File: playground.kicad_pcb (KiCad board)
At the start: 2 copper layers, 50 x 50 mm, 20 parts, among them IC1 TXU0101DBVR, IC3 TXU0101DBVR, IC4 TXU0101DBVR, IC5 TXU0101DBVR, IC6 TXU0101DBVR, IC7 TXU0101DBVR, IC8 TXU0101DBVR, J1 USB_A, SW1 SW_DIP_x01, U2 ATSAMD21G18A-A

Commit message: updates
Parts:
- removed J1: USB_A, Connector_USB:USB3_A_Receptacle_Wuerth_692122030100
- added C3: 10u, Capacitor_SMD:C_0805_2012Metric, F.Cu at (153.4, 64.9)
- added C4: 10u, Capacitor_SMD:C_0805_2012Metric, F.Cu at (153.4, 67.9)
- added C5: 100n, Capacitor_SMD:C_0805_2012Metric, F.Cu at (153.4, 71.0)
- added C6: 100n, Capacitor_SMD:C_0805_2012Metric, F.Cu at (153.4, 74.0)
- added C7: 33p, Capacitor_SMD:C_0805_2012Metric, F.Cu at (153.4, 77.0)
- added C8: 22u, Capacitor_SMD:C_0805_2012Metric, F.Cu at (153.4, 80.0)
- added C9: 100n, Capacitor_SMD:C_0805_2012Metric, F.Cu at (153.4, 83.0)
- added IC10: TPS562242DRLR, Package_SO:MSOP-10_3x3mm_P0.5mm, F.Cu at (156.8, 96.0)
- added IC2: TXU0101DBVR, custom_footprints:TXU0101DBVR, F.Cu at (142.8, 83.8)
- added IC9: L293DD, custom_footprints:SOIC127P1032X265-20N, F.Cu at (167.0, 69.5)
- added J2: Pump, custom_footprints:470531000, F.Cu at (134.0, 55.4)
- added J3: Fan, custom_footprints:470531000, F.Cu at (147.0, 55.5)
- added J4: Valve, custom_footprints:470531000, F.Cu at (160.0, 55.5)
- added J6: MOLEX POWER CONNECTOR, custom_footprints:455580003, F.Cu at (164.3, 81.3)
- added J7: USB_A, Connector_USB:USB_A_Molex_67643_Horizontal, F.Cu at (118.1, 64.5)
- added L1: 3u3, Inductor_SMD:L_0805_2012Metric, F.Cu at (127.5, 89.5)
- added R4: 100k, Resistor_SMD:R_0805_2012Metric, F.Cu at (157.9, 64.9)
- added R5: 11k3, Resistor_SMD:R_0805_2012Metric, F.Cu at (157.9, 67.8)
- added R6: 158k, Resistor_SMD:R_0805_2012Metric, F.Cu at (157.9, 70.8)
- added R7: 30k, Resistor_SMD:R_0805_2012Metric, F.Cu at (157.9, 73.8)
- C1, C2: footprint Capacitor_SMD:CP_Elec_8x10 -> Capacitor_SMD:C_0805_2012Metric
- moved IC8 41.0 mm to (147.6, 88.0)
- moved C2 39.0 mm to (107.5, 76.5), turned to -90 degrees
- moved SW1 38.5 mm to (105.5, 89.0)
- moved IC7 35.4 mm to (147.6, 83.8)
- moved IC1 34.7 mm to (142.8, 79.5)
- moved IC5 28.7 mm to (142.8, 96.5)
- moved C1 26.5 mm to (110.5, 76.5), turned to -90 degrees
- moved IC3 25.3 mm to (142.8, 88.0)
- moved IC6 23.9 mm to (147.6, 79.5)
- moved IC4 18.8 mm to (142.8, 92.3)
- moved D5 16.5 mm to (107.2, 72.1), turned to -90 degrees
- moved D1 10.2 mm to (119.3, 72.1), turned to -90 degrees
- moved R3 10.2 mm to (113.5, 76.5), turned to -90 degrees
- moved D4 8.97 mm to (110.2, 72.1), turned to -90 degrees
- moved D2 8.31 mm to (116.3, 72.1), turned to -90 degrees
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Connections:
- IC1 pad 1: +3V3 -> +5V
- IC1 pad 3: /PumpCtrl_3v3 -> /PumpSense_5v
- IC1 pad 4: /PumpCtrl_5v -> /PumpSense_3v3
- IC1 pad 5: +5V -> +3V3
- IC1 pad 6: +5V -> +3V3
- IC3 pad 1: +3V3 -> +5V
- IC3 pad 3: /ValveCtrl1_3v3 -> /ValveSense1_5v
- IC3 pad 4: /ValveCtrl1_5v -> /ValveSense1_3v3
- IC3 pad 5: +5V -> +3V3
- IC3 pad 6: +5V -> +3V3
- IC4 pad 1: +3V3 -> +5V
- IC4 pad 3: /ValveCtrl2_3v3 -> /ValveSense2_5v
- IC4 pad 4: /ValveCtrl2_5v -> /ValveSense2_3v3
- IC4 pad 5: +5V -> +3V3
- IC4 pad 6: +5V -> +3V3
- IC5 pad 1: +5V -> +3V3
- IC5 pad 3: /PumpSense_5v -> /PumpCtrl_3v3
- IC5 pad 4: /PumpSense_3v3 -> /PumpCtrl_5v
- IC5 pad 5: +3V3 -> +5V
- IC5 pad 6: +3V3 -> +5V
- IC6 pad 1: +5V -> +3V3
- IC6 pad 3: /FanSense_5v -> /FanCtrl_3v3
- IC6 pad 4: /FanSense_3v3 -> /FanCtrl_5v
- IC6 pad 5: +3V3 -> +5V
- IC6 pad 6: +3V3 -> +5V
- IC7 pad 1: +5V -> +3V3
- IC7 pad 3: /ValveSense1_5v -> /ValveCtrl1_3v3
- IC7 pad 4: /ValveSense1_3v3 -> /ValveCtrl1_5v
- IC7 pad 5: +3V3 -> +5V
- IC7 pad 6: +3V3 -> +5V
- IC8 pad 1: +5V -> +3V3
- IC8 pad 3: /ValveSense2_5v -> /ValveCtrl2_3v3
- IC8 pad 4: /ValveSense2_3v3 -> /ValveCtrl2_5v
- IC8 pad 5: +3V3 -> +5V
- IC8 pad 6: +3V3 -> +5V
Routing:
- net GND: track 2.60 -> 0.00 mm
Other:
- board size 50 x 50 mm -> 80 x 50 mm

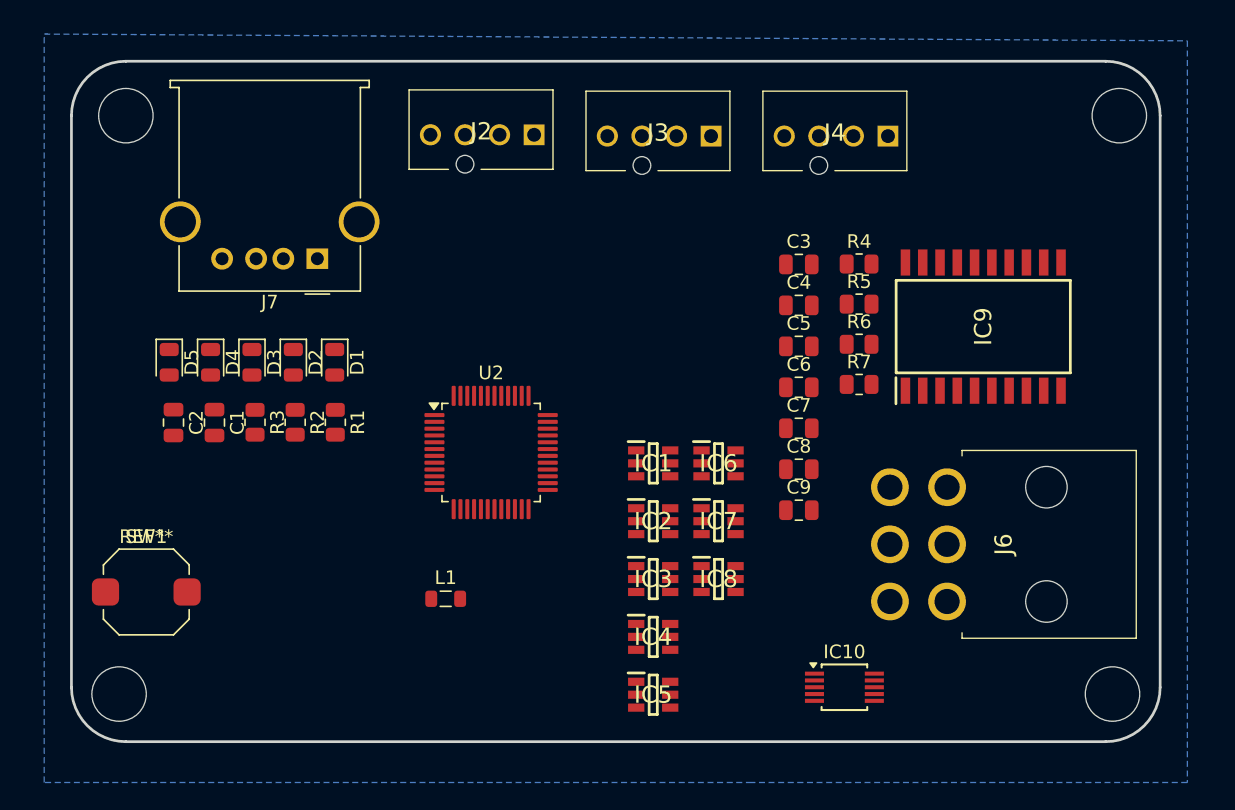
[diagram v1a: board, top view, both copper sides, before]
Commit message: did basic routing. Still missing some parts.
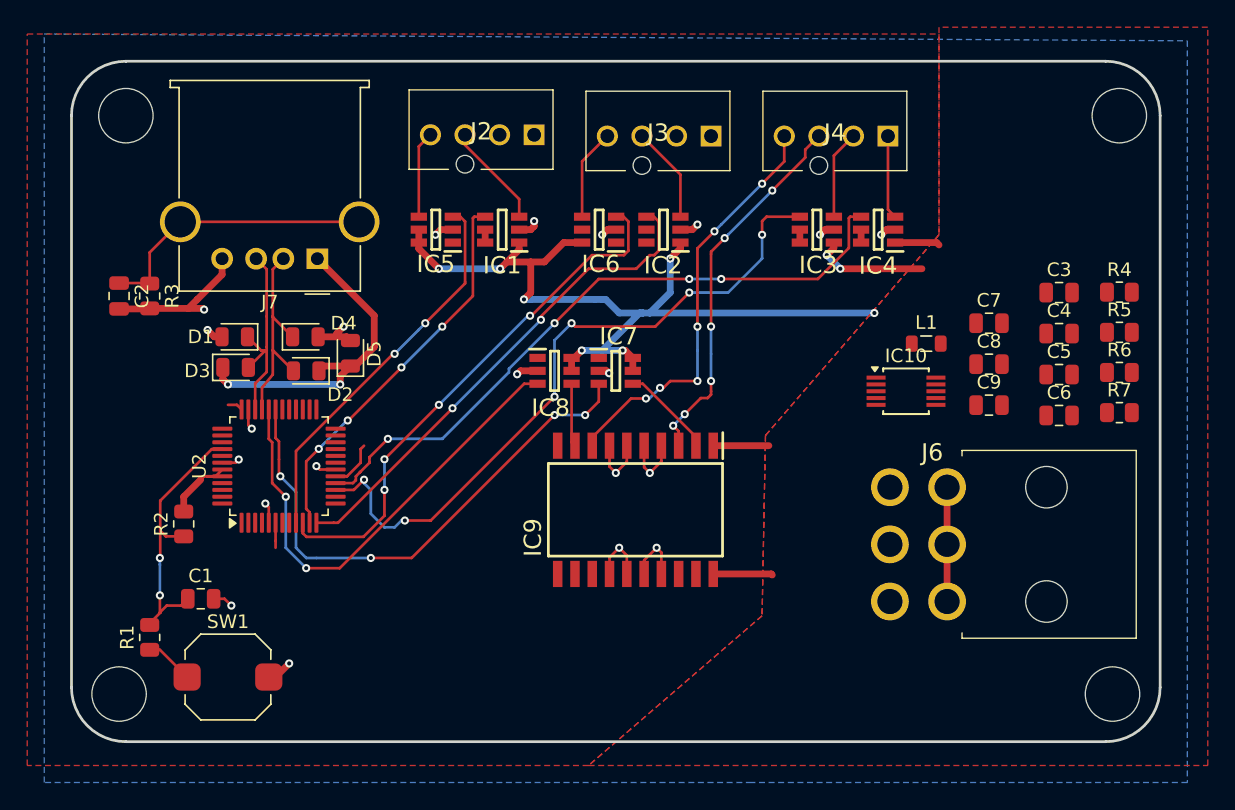
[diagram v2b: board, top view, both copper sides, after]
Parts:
- moved L1 40.0 mm to (162.8, 70.8)
- moved IC5 37.7 mm to (126.8, 62.4), turned to 180 degrees
- moved IC4 34.2 mm to (159.3, 62.4), turned to 180 degrees
- moved IC9 28.9 mm to (141.4, 83.0), turned to -90 degrees
- moved IC3 28.4 mm to (154.8, 62.4), turned to 180 degrees
- moved IC10 22.2 mm to (161.3, 74.2)
- moved IC2 21.4 mm to (143.5, 62.4), turned to 180 degrees
- moved R1 20.9 mm to (105.8, 92.3), turned to 90 degrees
- moved IC1 20.4 mm to (131.7, 62.4), turned to 180 degrees
- moved IC8 19.5 mm to (135.5, 72.8)
- moved IC6 19.3 mm to (138.8, 62.4), turned to 180 degrees
- moved C3 19.2 mm to (172.6, 67.0)
- moved C4 19.2 mm to (172.6, 70.0)
- moved C5 19.2 mm to (172.6, 73.0)
- moved C6 19.2 mm to (172.6, 76.0)
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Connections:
- D1 pad 1: +5V -> /USB_VBUS
- D2 pad 1: +5V -> /USB_VBUS
- D5 pad 1: +5V -> /USB_VBUS
- IC9 pad 3: /ValveOutput1_5v -> /ValveOutput1_12v
- IC9 pad 8: /ValveOutput2_5v -> /ValveOutput2_12v
- J4 pad 1: unconnected-(J4-Pad1) -> /ValveSense2_5v
- J4 pad 2: unconnected-(J4-Pad2) -> /ValveSense1_5v
- J4 pad 3: unconnected-(J4-Pad3) -> /ValveOutput1_12v
- J4 pad 4: unconnected-(J4-Pad4) -> /ValveOutput2_12v
- J7 pad 1: +5V -> /USB_VBUS
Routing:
- net +5V: track 0.00 -> 83.1 mm, vias 0 -> 9
- net GND: track 0.00 -> 54.2 mm, vias 0 -> 21
- net /ValveSense1_3v3: track 0.00 -> 50.7 mm, vias 0 -> 6
- net /ValveSense2_3v3: track 0.00 -> 48.8 mm, vias 0 -> 4
- net /ValveCtrl1_3v3: track 0.00 -> 39.4 mm, vias 0 -> 4
- net /FanCtrl_3v3: track 0.00 -> 39.1 mm, vias 0 -> 4
- net /FanSense_3v3: track 0.00 -> 36.8 mm, vias 0 -> 2
- net /ValveCtrl2_3v3: track 0.00 -> 35.4 mm, vias 0 -> 2
- net /ValveOutput2_12v: track 0.00 -> 30.7 mm, vias 0 -> 6
- net /PumpSense_3v3: track 0.00 -> 28.6 mm, vias 0 -> 4
- net /PumpCtrl_3v3: track 0.00 -> 28.4 mm, vias 0 -> 2
- net /ValveOutput1_12v: track 0.00 -> 27.6 mm, vias 0 -> 6
- net /USB_VBUS: track 0.00 -> 24.3 mm, vias 0 -> 2
- net /usb_shield_gnd: track 0.00 -> 20.9 mm
- net /RESET: track 0.00 -> 20.0 mm, vias 0 -> 2
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- added copper zone on F.Cu, net +3V3
- added copper zone on F.Cu, net +5V

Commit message: saving progress
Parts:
- removed IC10: TPS562242DRLR, Package_SO:MSOP-10_3x3mm_P0.5mm
- removed L1: 3u3, Inductor_SMD:L_0805_2012Metric
- added C10: 10u, Capacitor_SMD:C_0805_2012Metric, F.Cu at (146.0, 90.2)
- added C11: 10u, Capacitor_SMD:C_0805_2012Metric, F.Cu at (149.0, 90.2)
- added C12: 20p, Capacitor_SMD:C_0805_2012Metric, F.Cu at (124.2, 78.8)
- added C13: 20p, Capacitor_SMD:C_0805_2012Metric, F.Cu at (124.2, 81.2)
- added D10: FAN_PWM_IND, LED_SMD:LED_0603_1608Metric, F.Cu at (145.6, 97.3)
- added D11: VALVE_OPEN_IND, LED_SMD:LED_0603_1608Metric, F.Cu at (148.2, 97.3)
- added D12: VALVE_CLOSED_IND, LED_SMD:LED_0603_1608Metric, F.Cu at (150.8, 97.3)
- added D13: GENERAL_BOARD_1_IND, LED_SMD:LED_0603_1608Metric, F.Cu at (153.4, 97.3)
- added D14: GENERAL_BOARD_1_IND, LED_SMD:LED_0603_1608Metric, F.Cu at (156.0, 97.3)
- added D6: 5V_USB_PWR_IND, LED_SMD:LED_0603_1608Metric, F.Cu at (164.0, 96.5)
- added D7: 3v3_PWR_IND, LED_SMD:LED_0603_1608Metric, F.Cu at (137.9, 97.3)
- added D8: 12v_PWR_IND, LED_SMD:LED_0603_1608Metric, F.Cu at (140.5, 97.3)
- added D9: PUMP_PWM_IND, LED_SMD:LED_0603_1608Metric, F.Cu at (143.1, 97.3)
- added IC11: LM3940IMP-3.3_NOPB, custom_footprints:SOT230P700X180-4N, F.Cu at (129.8, 68.2)
- added J5: Conn_02x05_Counter_Clockwise, Connector_PinHeader_2.54mm:PinHeader_2x05_P2.54mm_Vertical_SMD, F.Cu at (122.7, 92.0)
- added JP1: SolderJumper_2_Open, Jumper:SolderJumper-2_P1.3mm_Open_Pad1.0x1.5mm, F.Cu at (118.8, 79.8)
- added JP2: SolderJumper_2_Open, Jumper:SolderJumper-2_P1.3mm_Open_Pad1.0x1.5mm, F.Cu at (134.1, 74.8)
- added R8: 300R, Resistor_SMD:R_1206_3216Metric, F.Cu at (173.3, 67.5)
- added Y1: 32.768kHz, custom_footprints:FC135327680KAA5, F.Cu at (128.0, 80.0)
- C1: value C -> 100n
- C3: value 10u -> 4.7n
- C4: value 10u -> 100n
- C5: value 100n -> 47u
- C7: value 33p -> 100n
- C8: value 22u -> 1u
- C9: value 100n -> 1u
- J7: footprint Connector_USB:USB_A_Molex_67643_Horizontal -> custom_footprints:676432910
- R4: value 100k -> 1k
- R5: value 11k3 -> 51R
- R6: value 158k -> 470R
- R7: value 30k -> 470R
- moved C5 59.9 mm to (112.8, 76.8)
- moved R4 55.0 mm to (130.7, 96.5)
- moved R3 54.9 mm to (155.2, 91.0), turned to 90 degrees
- moved C2 47.6 mm to (147.2, 86.1), turned to 0 degrees
- moved C3 43.6 mm to (129.5, 74.0)
- moved C6 41.1 mm to (133.9, 90.2), turned to 90 degrees
- moved C1 38.2 mm to (147.2, 83.1)
- moved C7 37.0 mm to (137.0, 90.2), turned to 90 degrees
- moved IC5 36.7 mm to (154.8, 86.2), turned to 0 degrees
- moved C8 32.8 mm to (140.0, 90.2), turned to 90 degrees
- moved C4 28.8 mm to (152.5, 90.7), turned to 90 degrees
- moved C9 28.6 mm to (143.0, 90.2), turned to 90 degrees
- moved U2 20.6 mm to (135.8, 82.0), turned to 0 degrees
- moved IC4 20.1 mm to (154.8, 82.0), turned to 0 degrees
- moved IC9 19.8 mm to (157.2, 70.9), turned to 90 degrees
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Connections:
- C3 pad 1: +12V -> /LDO_POWER_IN
- C4 pad 1: +12V -> +3V3
- C5 pad 1: +12V -> /LDO_POWER_OUT
- C6 pad 1: /Power Regulation/buck_sw -> +3V3
- C6 pad 2: Net-(IC10-BST) -> GND
- C7 pad 1: /Power Regulation/buck_fb -> +3V3
- C7 pad 2: +5V -> GND
- C8 pad 1: GND -> +3V3
- C8 pad 2: +5V -> GND
- C9 pad 1: GND -> +3V3
- C9 pad 2: +5V -> GND
- D1 pad 1: /USB_VBUS -> +5V
- D2 pad 1: /USB_VBUS -> +5V
- D5 pad 1: /USB_VBUS -> +5V
- J7 pad 1: /USB_VBUS -> +5V
- R4 pad 1: +12V -> /SWCLK
- R4 pad 2: /Power Regulation/buck_en -> +3V3
- R5 pad 1: /Power Regulation/buck_en -> GND
- R5 pad 2: GND -> +3V3
- R6 pad 1: +5V -> Net-(R6-Pad1)
- R6 pad 2: /Power Regulation/buck_fb -> +12V
- R7 pad 1: /Power Regulation/buck_fb -> Net-(R6-Pad1)
- U2 pad 1: unconnected-(U2-PA00-Pad1) -> /XIN32
- U2 pad 2: unconnected-(U2-PA01-Pad2) -> /XOUT32
- U2 pad 45: unconnected-(U2-PA30-Pad45) -> /SWCLK
- U2 pad 46: unconnected-(U2-PA31-Pad46) -> /SWDIO
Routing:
- net +5V: track 83.1 -> 0.00 mm, vias 9 -> 0
- net GND: track 54.2 -> 0.00 mm, vias 21 -> 0
- net /ValveSense1_3v3: track 50.7 -> 0.00 mm, vias 6 -> 0
- net /ValveSense2_3v3: track 48.8 -> 0.00 mm, vias 4 -> 0
- net /ValveCtrl1_3v3: track 39.4 -> 0.00 mm, vias 4 -> 0
- net /FanCtrl_3v3: track 39.1 -> 0.00 mm, vias 4 -> 0
- net /FanSense_3v3: track 36.8 -> 0.00 mm, vias 2 -> 0
- net /ValveCtrl2_3v3: track 35.4 -> 0.00 mm, vias 2 -> 0
- net /ValveOutput2_12v: track 30.7 -> 0.00 mm, vias 6 -> 0
- net /PumpSense_3v3: track 28.6 -> 0.00 mm, vias 4 -> 0
- net /PumpCtrl_3v3: track 28.4 -> 0.00 mm, vias 2 -> 0
- net /ValveOutput1_12v: track 27.6 -> 0.00 mm, vias 6 -> 0
- net /USB_VBUS: track 24.3 -> 0.00 mm, vias 2 -> 0
- net /usb_shield_gnd: track 20.9 -> 0.00 mm
- net /RESET: track 20.0 -> 0.00 mm, vias 2 -> 0
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- removed copper zone on F.Cu, net +3V3
- removed copper zone on F.Cu, net +5V
- removed copper zone on B.Cu, net GND
